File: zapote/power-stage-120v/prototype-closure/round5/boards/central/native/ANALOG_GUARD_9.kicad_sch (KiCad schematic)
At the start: 6 parts, among them U24 SN74LVC1G08DBVR, U25 SN74LVC1G08DBVR, U26 SN74LVC1G08DBVR

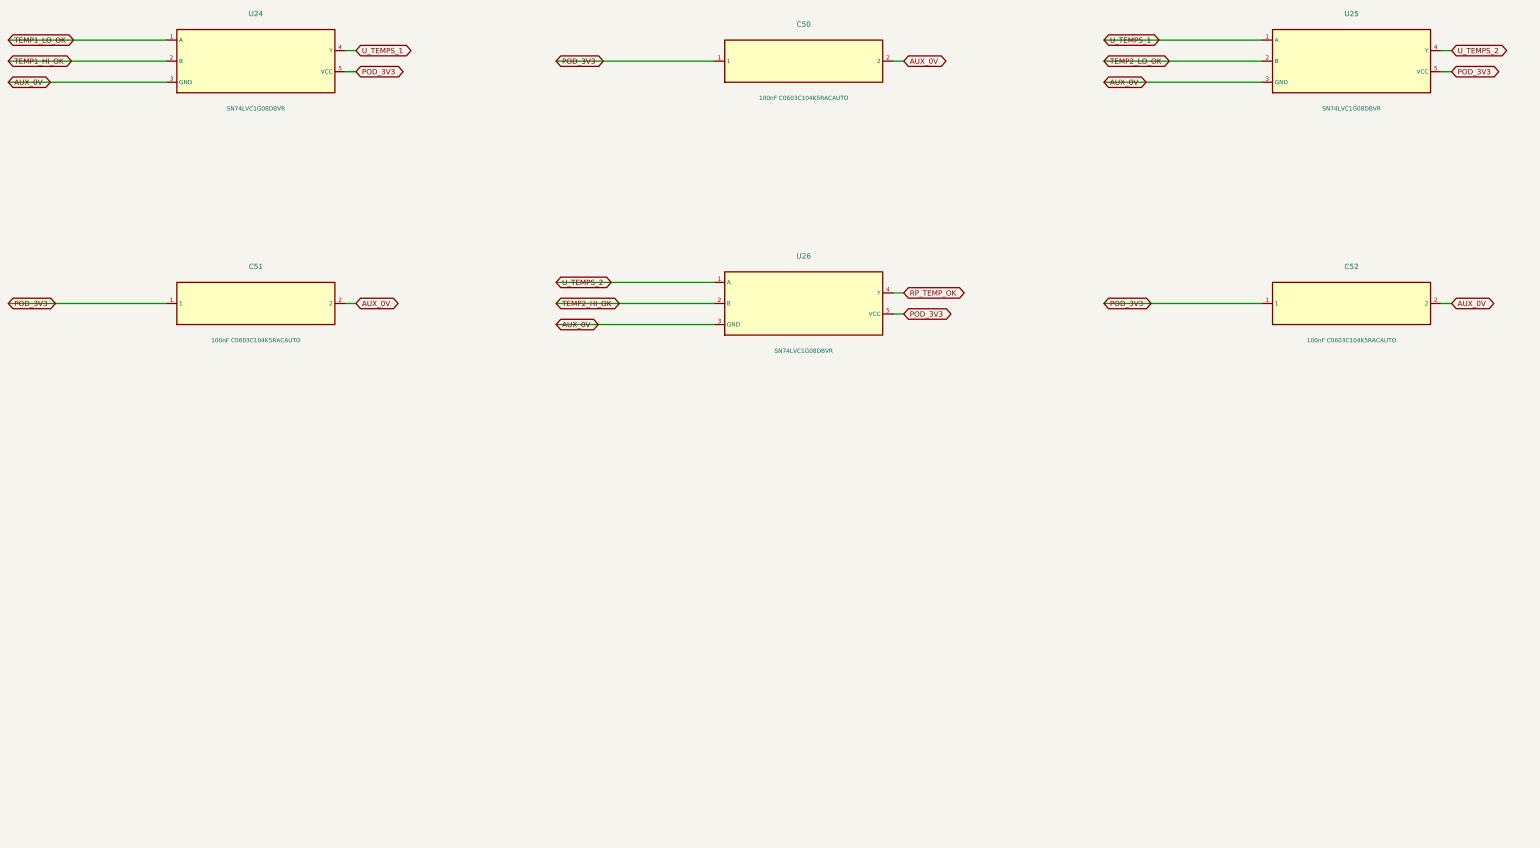
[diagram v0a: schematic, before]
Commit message: WIP snapshot of worktrees/mit-product-guidance (2026-10-08)
Uncommitted Codex prototype-closure work (round5 boards, round6
investigation, firmware power adapter), snapshotted without touching the
worktree. Raw solver output under output/temper-prototype-closure/ is
not included.

Co-Authored-By: Claude Opus 5.5 (1M context) <noreply@anthropic.com>
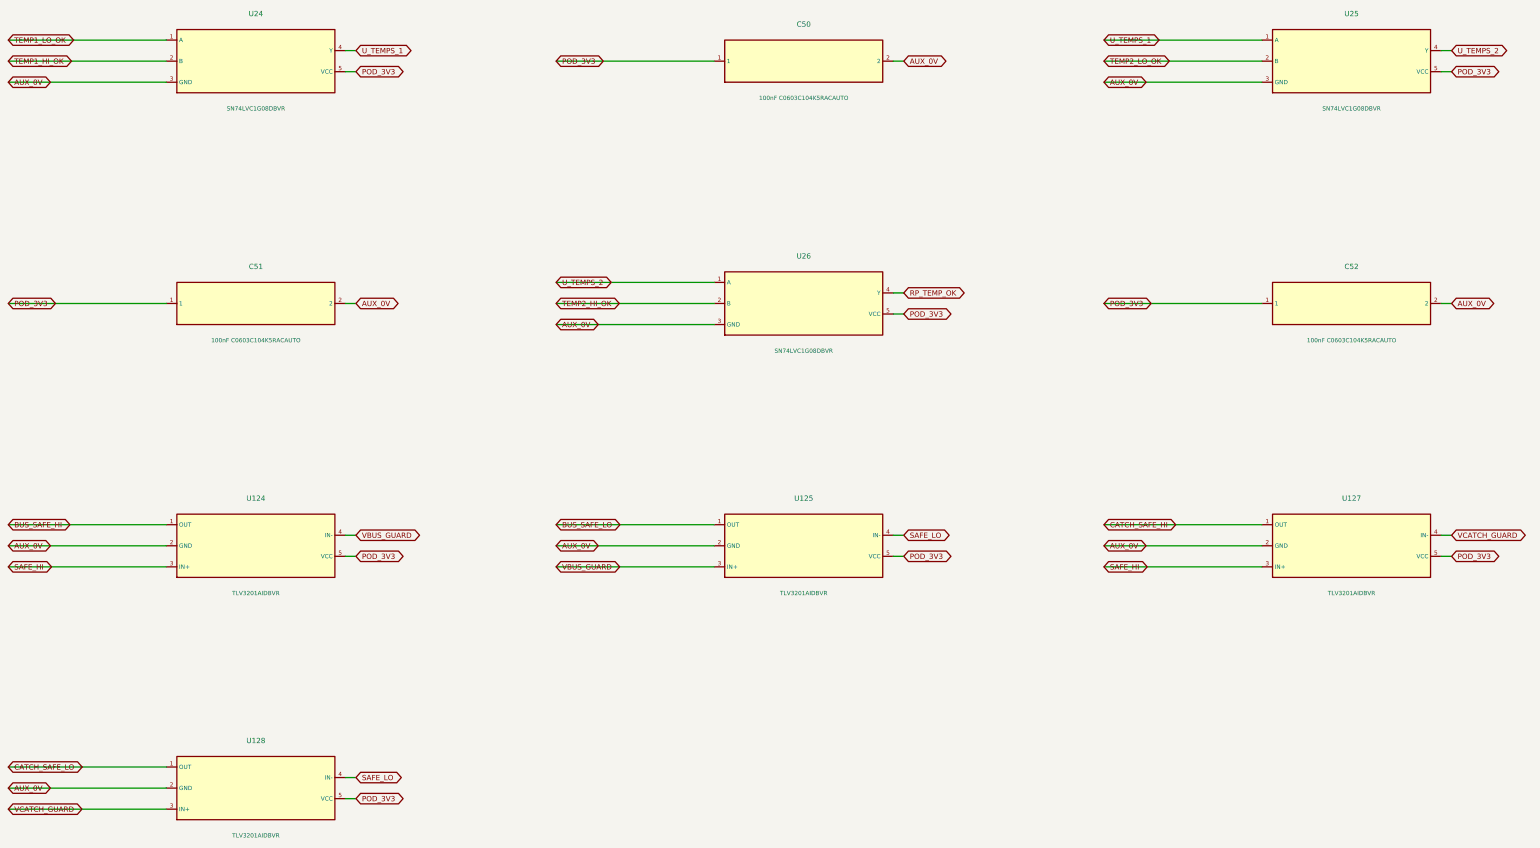
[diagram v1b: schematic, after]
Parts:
- added U124: TLV3201AIDBVR, Package_TO_SOT_SMD:SOT-23-5, symbol Supervisor:Part_U124
- added U125: TLV3201AIDBVR, Package_TO_SOT_SMD:SOT-23-5, symbol Supervisor:Part_U125
- added U127: TLV3201AIDBVR, Package_TO_SOT_SMD:SOT-23-5, symbol Supervisor:Part_U127
- added U128: TLV3201AIDBVR, Package_TO_SOT_SMD:SOT-23-5, symbol Supervisor:Part_U128
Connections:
- net AUX_0V: now also U124.2 (GND), U125.2 (GND), U127.2 (GND), U128.2 (GND)
- net POD_3V3: now also U124.5 (VCC), U125.5 (VCC), U127.5 (VCC), U128.5 (VCC)
- new net BUS_SAFE_HI: U124.1 (OUT)
- new net BUS_SAFE_LO: U125.1 (OUT)
- new net CATCH_SAFE_HI: U127.1 (OUT)
- new net CATCH_SAFE_LO: U128.1 (OUT)
- new net SAFE_HI: U124.3 (IN+), U127.3 (IN+)
- new net SAFE_LO: U125.4 (IN-), U128.4 (IN-)
- new net VBUS_GUARD: U124.4 (IN-), U125.3 (IN+)
- new net VCATCH_GUARD: U127.4 (IN-), U128.3 (IN+)
